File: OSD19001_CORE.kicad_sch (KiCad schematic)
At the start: 14 parts, among them U1 ${PARTNUMBER}, Y1 ${FREQUENCY}

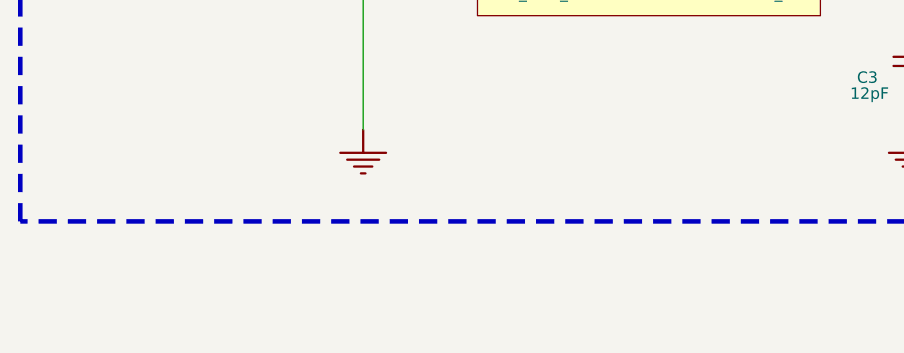
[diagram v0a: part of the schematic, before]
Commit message: Added PWR FLAGS. Passes ERC, no errors or warnings
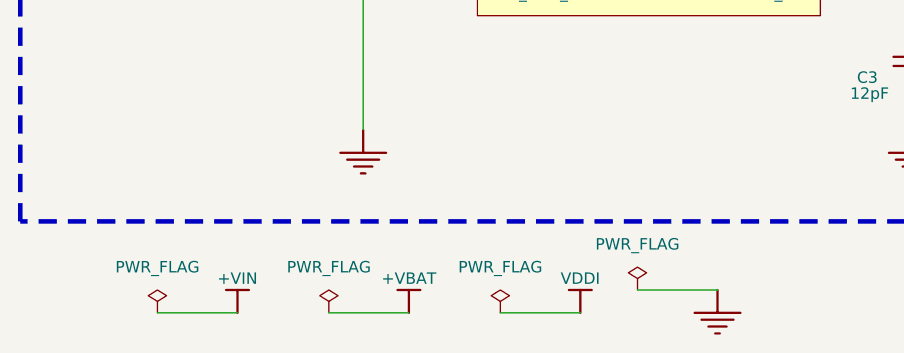
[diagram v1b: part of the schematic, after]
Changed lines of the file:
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@@
     (stroke (width 0.254) (type solid) (color 0 0 0 0))
+  )
+  (wire (pts (xy 38.1 274.32) (xy 46.99 274.32))
+    (stroke (width 0) (type solid) (color 0 0 0 0))
   )
   (wire (pts (xy 48.26 76.2) (xy 48.26 78.74))
@@
     (stroke (width 0.254) (type solid) (color 0 0 0 0))
   )
+  (wire (pts (xy 57.15 274.32) (xy 66.04 274.32))
+    (stroke (width 0) (type solid) (color 0 0 0 0))
+  )
   (wire (pts (xy 60.96 76.2) (xy 60.96 73.66))
     (stroke (width 0.254) (type solid) (color 0 0 0 0))
@@
   (wire (pts (xy 68.58 231.14) (xy 53.34 231.14))
     (stroke (width 0.254) (type solid) (color 0 0 0 0))
+  )
+  (wire (pts (xy 76.2 274.32) (xy 85.09 274.32))
+    (stroke (width 0) (type solid) (color 0 0 0 0))
+  )
+  (wire (pts (xy 91.44 271.78) (xy 100.33 271.78))
+    (stroke (width 0) (type solid) (color 0 0 0 0))
   )
   (wire (pts (xy 116.84 78.74) (xy 129.54 78.74))
@@
     (effects (font (size 1.27 1.27)) (justify right))
   )
+  (symbol (lib_id "power:PWR_FLAG") (at 38.1 274.32 0) (unit 1)
+    (in_bom yes) (on_board yes) (fields_autoplaced)
+    (property "Reference" "#FLG0105" (id 0) (at 38.1 272.415 0)
+      (effects (font (size 1.27 1.27)) hide)
+    )
+    (property "Value" "PWR_FLAG" (id 1) (at 38.1 269.24 0))
+    (property "Footprint" "" (id 2) (at 38.1 274.32 0)
+      (effects (font (size 1.27 1.27)) hide)
+    )
+    (property "Datasheet" "~" (id 3) (at 38.1 274.32 0)
+      (effects (font (size 1.27 1.27)) hide)
+    )
+    (pin "1")
+  )
+  (symbol (lib_id "power:PWR_FLAG") (at 57.15 274.32 0) (unit 1)
+    (in_bom yes) (on_board yes) (fields_autoplaced)
+    (property "Reference" "#FLG0106" (id 0) (at 57.15 272.415 0)
+      (effects (font (size 1.27 1.27)) hide)
+    )
+    (property "Value" "PWR_FLAG" (id 1) (at 57.15 269.24 0))
+    (property "Footprint" "" (id 2) (at 57.15 274.32 0)
+      (effects (font (size 1.27 1.27)) hide)
+    )
+    (property "Datasheet" "~" (id 3) (at 57.15 274.32 0)
+      (effects (font (size 1.27 1.27)) hide)
+    )
+    (pin "1")
+  )
+  (symbol (lib_id "power:PWR_FLAG") (at 76.2 274.32 0) (unit 1)
+    (in_bom yes) (on_board yes) (fields_autoplaced)
+    (property "Reference" "#FLG0107" (id 0) (at 76.2 272.415 0)
+      (effects (font (size 1.27 1.27)) hide)
+    )
+    (property "Value" "PWR_FLAG" (id 1) (at 76.2 269.24 0))
+    (property "Footprint" "" (id 2) (at 76.2 274.32 0)
+      (effects (font (size 1.27 1.27)) hide)
+    )
+    (property "Datasheet" "~" (id 3) (at 76.2 274.32 0)
+      (effects (font (size 1.27 1.27)) hide)
+    )
+    (pin "1")
+  )
+  (symbol (lib_id "power:PWR_FLAG") (at 91.44 271.78 0) (unit 1)
+    (in_bom yes) (on_board yes) (fields_autoplaced)
+    (property "Reference" "#FLG?" (id 0) (at 91.44 269.875 0)
+      (effects (font (size 1.27 1.27)) hide)
+    )
+    (property "Value" "PWR_FLAG" (id 1) (at 91.44 266.7 0))
+    (property "Footprint" "" (id 2) (at 91.44 271.78 0)
+      (effects (font (size 1.27 1.27)) hide)
+    )
+    (property "Datasheet" "~" (id 3) (at 91.44 271.78 0)
+      (effects (font (size 1.27 1.27)) hide)
+    )
+    (pin "1")
+  )
   (symbol (lib_id "OSD19001_CORE-altium-import:+3.3V") (at 35.56 73.66 180) (unit 1)
     (in_bom yes) (on_board yes)
@@
     (pin "")
   )
+  (symbol (lib_id "OSD19001_CORE-altium-import:+VIN") (at 46.99 274.32 180) (unit 1)
+    (in_bom yes) (on_board yes)
+    (property "Reference" "#PWR0105" (id 0) (at 46.99 274.32 0)
+      (effects (font (size 1.27 1.27)) hide)
+    )
+    (property "Value" "+VIN" (id 1) (at 46.99 270.51 0))
+    (property "Footprint" "" (id 2) (at 46.99 274.32 0)
+      (effects (font (size 1.27 1.27)) hide)
+    )
+    (property "Datasheet" "" (id 3) (at 46.99 274.32 0)
+      (effects (font (size 1.27 1.27)) hide)
+    )
+    (pin "")
+  )
   (symbol (lib_id "OSD19001_CORE-altium-import:+VIN") (at 60.96 73.66 180) (unit 1)
     (in_bom yes) (on_board yes)
@@
     (pin "")
   )
+  (symbol (lib_id "OSD19001_CORE-altium-import:+VBAT") (at 66.04 274.32 180) (unit 1)
+    (in_bom yes) (on_board yes)
+    (property "Reference" "#PWR0106" (id 0) (at 66.04 274.32 0)
+      (effects (font (size 1.27 1.27)) hide)
+    )
+    (property "Value" "+VBAT" (id 1) (at 66.04 270.51 0))
+    (property "Footprint" "" (id 2) (at 66.04 274.32 0)
+      (effects (font (size 1.27 1.27)) hide)
+    )
+    (property "Datasheet" "" (id 3) (at 66.04 274.32 0)
+      (effects (font (size 1.27 1.27)) hide)
+    )
+    (pin "")
+  )
+  (symbol (lib_id "OSD19001_CORE-altium-import:VDDI") (at 85.09 274.32 180) (unit 1)
+    (in_bom yes) (on_board yes)
+    (property "Reference" "#PWR0107" (id 0) (at 85.09 274.32 0)
+      (effects (font (size 1.27 1.27)) hide)
+    )
+    (property "Value" "VDDI" (id 1) (at 85.09 270.51 0))
+    (property "Footprint" "" (id 2) (at 85.09 274.32 0)
+      (effects (font (size 1.27 1.27)) hide)
+    )
+    (property "Datasheet" "" (id 3) (at 85.09 274.32 0)
+      (effects (font (size 1.27 1.27)) hide)
+    )
+    (pin "")
+  )
   (symbol (lib_id "OSD19001_CORE-altium-import:+3.3V") (at 129.54 73.66 180) (unit 1)
     (in_bom yes) (on_board yes)
@@
       (effects (font (size 1.27 1.27)) hide)
     )
+    (pin "")
+  )
+  (symbol (lib_id "OSD19001_CORE-altium-import:GND") (at 100.33 271.78 0) (unit 1)
+    (in_bom yes) (on_board yes)
+    (property "Reference" "#PWR?" (id 0) (at 100.33 271.78 0)
+      (effects (font (size 1.27 1.27)) hide)
+    )
+    (property "Value" "GND" (id 1) (at 100.33 278.13 0)
+      (effects (font (size 1.27 1.27)) hide)
+    )
+    (property "Footprint" "" (id 2) (at 100.33 271.78 0)
+      (effects (font (size 1.27 1.27)) hide)
+    )
+    (property "Datasheet" "" (id 3) (at 100.33 271.78 0)
+      (effects (font (size 1.27 1.27)) hide)
+    )
